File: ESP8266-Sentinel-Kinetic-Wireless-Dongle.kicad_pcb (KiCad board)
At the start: 2 copper layers, 39.7 x 60.1 mm, 61 parts, among them J1 Conn_01x04, J2 Screw_Terminal_01x04, J3 Conn_01x06_Pin, J4 RJ9, J5 Screw_Terminal_01x03, J6 Screw_Terminal_01x04, Q1 SS8050, Q2 AO3401A, Q3 AO3400A, SW2 SW_Push, SW4 SW_Push, U1 AMS1117-3.3, U2 ESP-12E, U3 MAX3232, U4 ESP32-WROOM-32, U5 L78L10_SOT89, U6 74AHCT125

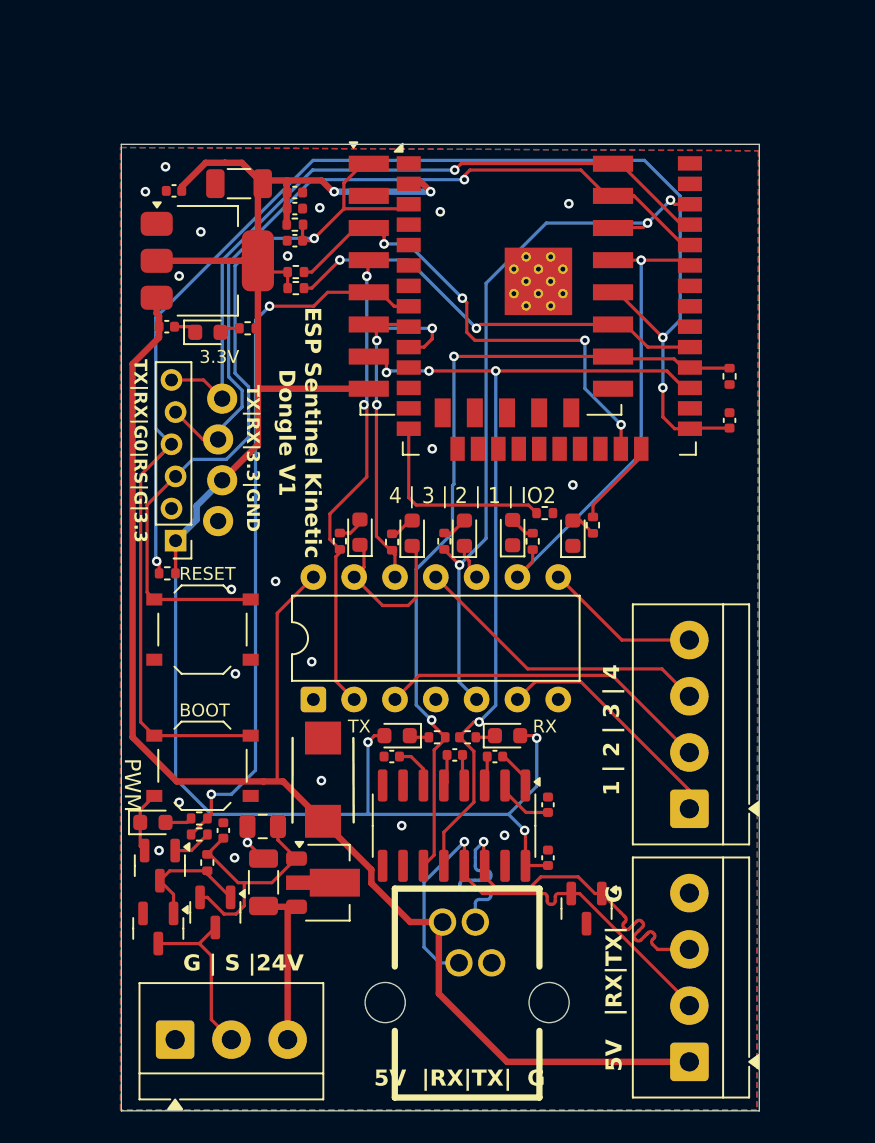
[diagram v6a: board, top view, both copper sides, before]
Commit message: Layout completed Revesed RJ9 pinout to match Display Module Added reverse polarity protection diode to 24V rail Using OpAMP for 3.3 to 5V conversion Using OpAmp for 3.3 to 10V conversion JST XH for Mode 02 Control instead of screw terminals Added 5v 3A Buck regulator PMOD connector for spare GPIO Added I2C header
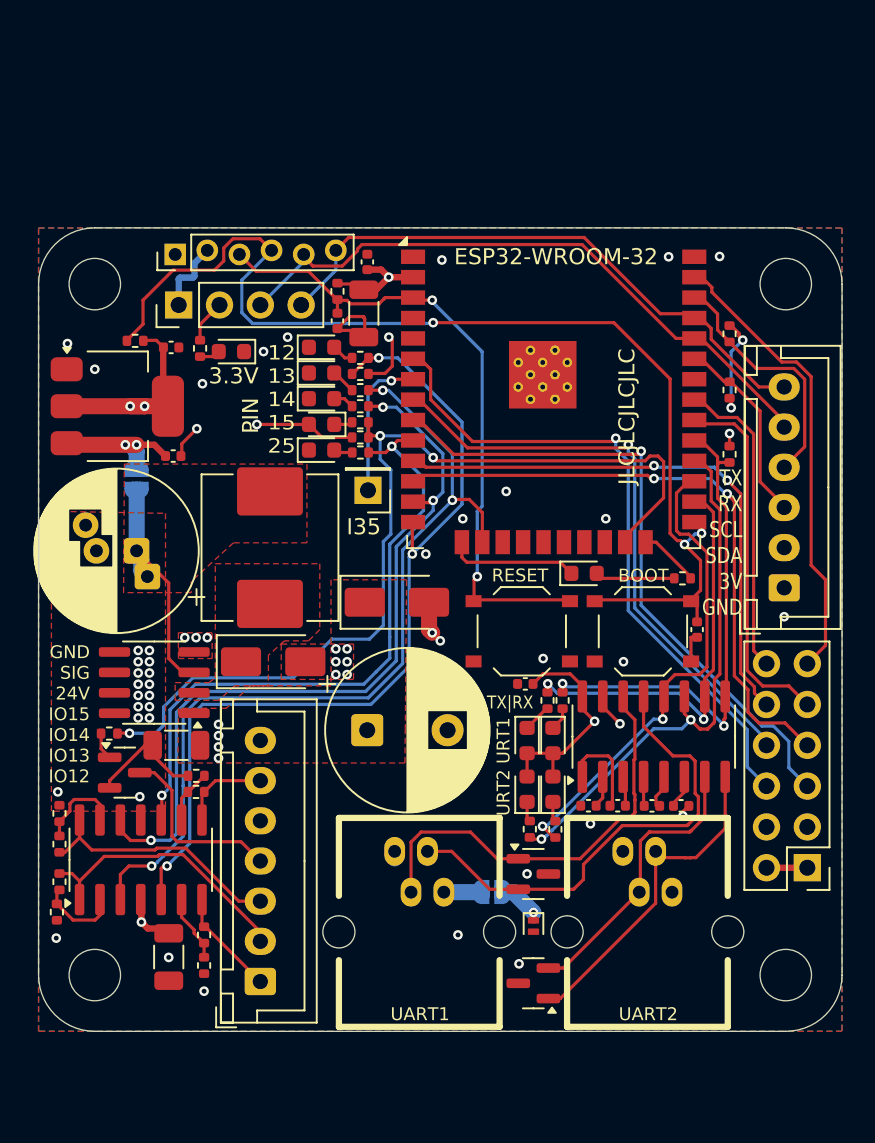
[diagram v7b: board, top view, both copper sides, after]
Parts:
- removed C14: 22uF, Capacitor_SMD:C_0805_2012Metric
- removed C15: 100n, Capacitor_SMD:C_0402_1005Metric
- removed G1: OSHW_Logo, SparkFun-Aesthetic:Creative_Commons_License
- removed Q2: AO3401A, Package_TO_SOT_SMD:SOT-23
- removed Q3: AO3400A, Package_TO_SOT_SMD:SOT-23
- removed SW4: SW_Push, Button_Switch_SMD:SW_Push_1P1T_XKB_TS-1187A
- removed U5: L78L10_SOT89, Package_TO_SOT_SMD:SOT-89-3
- removed U6: 74AHCT125, Package_DIP:DIP-14_W7.62mm
- added C16: 1u, Capacitor_SMD:C_1206_3216Metric, F.Cu at (133.6, 107.2)
- added C17: 82uF, Capacitor_THT:CP_Radial_D10.0mm_P2.50mm_P5.00mm, F.Cu at (131.1, 95.1)
- added D12: LED, LED_SMD:LED_0603_1608Metric, F.Cu at (142.6, 87.2)
- added D13: LED, LED_SMD:LED_0603_1608Metric, F.Cu at (157.0, 106.9)
- added D14: LED, LED_SMD:LED_0603_1608Metric, F.Cu at (155.4, 106.9)
- added D15: SSL34F, Diode_SMD:D_SMA, F.Cu at (139.6, 102.0)
- added D16: SSL34F, Diode_SMD:D_SMA, F.Cu at (147.3, 98.3)
- added H1: MountingHole, MountingHole:MountingHole_3.2mm_M3, F.Cu at (171.5, 78.5)
- added H2: MountingHole, MountingHole:MountingHole_3.2mm_M3, F.Cu at (171.5, 121.5)
- added H3: MountingHole, MountingHole:MountingHole_3.2mm_M3, F.Cu at (128.5, 121.5)
- added H4: MountingHole, MountingHole:MountingHole_3.2mm_M3, F.Cu at (128.5, 78.5)
- added J7: Conn_02x06_Odd_Even, Connector_PinHeader_2.54mm:PinHeader_2x06_P2.54mm_Vertical, F.Cu at (172.8, 114.8)
- added J8: Conn_01x07_Socket, Connector_JST:JST_XH_B7B-XH-A_1x07_P2.50mm_Vertical, F.Cu at (138.8, 121.9)
- added JP1: SolderJumper_2_Open, Jumper:SolderJumper-2_P1.3mm_Open_RoundedPad1.0x1.5mm, B.Cu at (153.2, 116.3)
- added JP2: SolderJumper_2_Open, Jumper:SolderJumper-2_P1.3mm_Open_RoundedPad1.0x1.5mm, B.Cu at (131.1, 90.7)
- added L1: 68uH/2A, Inductor_SMD:L_APV_APH0850, F.Cu at (139.4, 94.9)
- added R15: 10K, Resistor_SMD:R_0402_1005Metric, F.Cu at (134.8, 109.1)
- added R19: 1K, Resistor_SMD:R_0402_1005Metric, F.Cu at (157.6, 104.4)
- added R20: 1K, Resistor_SMD:R_0402_1005Metric, F.Cu at (156.7, 104.4)
- added R21: 2.2K, Resistor_SMD:R_0402_1005Metric, F.Cu at (168.0, 85.1)
- added R22: 2.2K, Resistor_SMD:R_0402_1005Metric, F.Cu at (168.0, 81.6)
- added R23: 5.1K, Resistor_SMD:R_0402_1005Metric, F.Cu at (135.3, 119.0)
- added R24: 10K, Resistor_SMD:R_0402_1005Metric, F.Cu at (126.1, 117.6)
- added R25: 5.1K, Resistor_SMD:R_0402_1005Metric, F.Cu at (126.3, 115.7)
- added R26: 10K, Resistor_SMD:R_0402_1005Metric, F.Cu at (126.3, 111.4)
- added R27: 5.1K, Resistor_SMD:R_0402_1005Metric, F.Cu at (126.3, 113.3)
- added SW1: SW_Push, Button_Switch_SMD:SW_Push_1P1T_XKB_TS-1187A, F.Cu at (155.1, 100.1)
- added U7: XL1509-5.0, Package_SO:SOIC-8_3.9x4.9mm_P1.27mm, F.Cu at (132.2, 103.3)
- C12: value 100uF -> 220uF; footprint Capacitor_SMD:C_1206_3216Metric -> Capacitor_THT:CP_Radial_D10.0mm_P5.00mm
- C13: value 10u -> 1u
- C4: value 10u -> 100uF; footprint Capacitor_SMD:C_0402_1005Metric -> Capacitor_SMD:C_1206_3216Metric
- D2: value P6SMB6.8CA-C78395 -> H5VL10B; footprint lib:SMB_L4.6-W3.6-LS5.3-BI -> Diode_SMD:D_SOD-882
- D8: value LED -> PSM712-LF-T7; footprint LED_SMD:LED_0603_1608Metric -> Package_TO_SOT_SMD:SOT-23
- J1: value Conn_01x04 -> RJ9; footprint SparkFun-Connector:1x04_Locking -> lib:RJ9-TH-623K-4P4CGRAYBOUNDLESS
- J2: value Screw_Terminal_01x04 -> RJ9; footprint TerminalBlock_4Ucon:TerminalBlock_4Ucon_1x04_P3.50mm_Horizontal -> lib:RJ9-TH-623K-4P4CGRAYBOUNDLESS
- J4: value RJ9 -> Conn_01x01_Pin; footprint lib:RJ9-TH-623K-4P4CGRAYBOUNDLESS -> Connector_PinHeader_2.54mm:PinHeader_1x01_P2.54mm_Vertical
- J5: value Screw_Terminal_01x03 -> Conn_01x04_Pin; footprint TerminalBlock_4Ucon:TerminalBlock_4Ucon_1x03_P3.50mm_Horizontal -> Connector_PinHeader_2.54mm:PinHeader_1x04_P2.54mm_Vertical
- J6: value Screw_Terminal_01x04 -> Conn_01x06_Pin; footprint TerminalBlock_4Ucon:TerminalBlock_4Ucon_1x04_P3.50mm_Horizontal -> Connector_JST:JST_XH_B6B-XH-A_1x06_P2.50mm_Vertical
- R14: value 1K -> 10K
- R16: value 1K -> 22K
- R5: value 10K -> 1K
- U2: value ESP-12E -> LM324; footprint lib:ESP-12E -> Package_SO:SOIC-14_3.9x8.7mm_P1.27mm
- moved J5 45.7 mm to (133.7, 79.8), turned to 90 degrees
- moved U2 45.4 mm to (131.4, 114.3), turned to 90 degrees
- moved C12 34.9 mm to (145.5, 106.3), turned to 0 degrees
- moved R12 28.9 mm to (129.4, 106.5), turned to 0 degrees
- moved R1 28.9 mm to (168.0, 89.1), turned to -90 degrees
- moved J4 28.8 mm to (145.5, 91.3), turned to 180 degrees
- moved SW2 28.7 mm to (162.6, 100.1)
- moved D8 28.1 mm to (155.8, 122.0), turned to 180 degrees
- moved D7 25.4 mm to (142.6, 88.8)
- moved J1 25.1 mm to (148.7, 115.1), turned to 0 degrees
- moved R11 24.9 mm to (145.0, 89.0)
- moved R5 23.2 mm to (145.0, 87.1), turned to 180 degrees
- moved C10 18.3 mm to (165.0, 111.0), turned to 0 degrees
- moved J3 17.9 mm to (133.5, 76.5), turned to 90 degrees
- moved D2 16.0 mm to (155.8, 118.5)
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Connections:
- C12 pad 1: +3.3V -> +24V
- C13 pad 1: VCC -> +24V
- D1 pad 1: /RS232_TX -> /RS_TX
- D1 pad 2: /RS232_RX -> /RS_RX
- D2 pad 1: GND -> +5V
- D2 pad 2: +5V -> GND
- D8 pad 1: GND -> /RS_RX2
- D8 pad 2: Net-(D8-A) -> /RS_TX2
- J1 pad 2: +3.3V -> /RS_TX
- J1 pad 3: /RX -> /RS_RX
- J1 pad 4: /TX -> Net-(JP1-A)
- J2 pad 1: +5V -> GND
- J2 pad 2: /RS232_RX -> /RS_TX2
- J2 pad 3: /RS232_TX -> /RS_RX2
- J2 pad 4: GND -> +5V
- J4 pad 1: +5V -> /IO35
- J5 pad 2: /10V_PWM -> +3.3V
- J5 pad 3: VCC -> /RX
- J6 pad 1: Net-(J6-Pin_1) -> GND
- J6 pad 2: Net-(J6-Pin_2) -> +3.3V
- J6 pad 3: Net-(J6-Pin_3) -> /SDA
- J6 pad 4: Net-(J6-Pin_4) -> /SCL
- Q1 pad 3: Net-(Q1-C) -> /OUT4
- R1 pad 2: /SH_1 -> /RX1
- R10 pad 1: /ALT_TX -> /TX2
- R12 pad 1: Net-(D8-A) -> Net-(Q1-B)
- R12 pad 2: /OUT1 -> /IO15
- R13 pad 2: /OUT2 -> /IO13
- R14 pad 1: /PWM -> GND
- R14 pad 2: Net-(Q1-B) -> Net-(U2B--)
- R16 pad 1: +10V -> /10V_PWM
- R16 pad 2: Net-(Q1-C) -> Net-(U2C--)
- R17 pad 2: /OUT3 -> /IO14
- R18 pad 2: /OUT4 -> /IO12
- R2 pad 2: /SH_2 -> /IO15
- R5 pad 1: GND -> /IO15
- R5 pad 2: /ALT_TX -> Net-(D12-K)
- R6 pad 2: /SL_1 -> /IO12
- R9 pad 1: /ALT_RX -> /RX2
- U2 pad 1: /RST -> /OUT2
- U2 pad 10: unconnected-(U2-MISO-Pad10) -> /PWM
- U2 pad 11: unconnected-(U2-GPIO9-Pad11) -> GND
- U2 pad 12: unconnected-(U2-GPIO10-Pad12) -> /IO14
- U2 pad 13: unconnected-(U2-MOSI-Pad13) -> Net-(U2D--)
- U2 pad 14: unconnected-(U2-SCLK-Pad14) -> /OUT3
- U2 pad 2: unconnected-(U2-ADC-Pad2) -> Net-(U2A--)
- U2 pad 3: /SH_2 -> /IO13
- U2 pad 4: /OUT4 -> +24V
- U2 pad 5: /PWM -> /IO12
- U2 pad 6: /OUT3 -> Net-(U2B--)
- U2 pad 7: /ALT_RX -> /OUT1
- U2 pad 8: +3.3V -> /10V_PWM
- U3 pad 10: GND -> /TX1
- U3 pad 11: /ALT_TX -> /TX2
- U3 pad 12: /ALT_RX -> /RX2
- U3 pad 13: /RS232_RX -> /RS_RX
- U3 pad 14: /RS232_TX -> /RS_TX
- U3 pad 7: unconnected-(U3-T2OUT-Pad7) -> /RS_TX2
- U3 pad 8: GND -> /RS_RX2
- U3 pad 9: unconnected-(U3-R2OUT-Pad9) -> /RX1
- U4 pad 10: /OUT4 -> /PWM
- U4 pad 11: unconnected-(U4-IO26-Pad11) -> /IO26
- U4 pad 12: unconnected-(U4-IO27-Pad12) -> /IO27
- U4 pad 13: unconnected-(U4-IO14-Pad13) -> /IO14
- U4 pad 14: /SL_1 -> /IO12
- U4 pad 16: unconnected-(U4-IO13-Pad16) -> /IO13
- U4 pad 23: /SH_2 -> /IO15
- U4 pad 26: unconnected-(U4-IO4-Pad26) -> /TX1
- U4 pad 27: /ALT_RX -> /RX2
- U4 pad 28: /ALT_TX -> /TX2
- U4 pad 29: /SH_1 -> /RX1
- U4 pad 30: unconnected-(U4-IO18-Pad30) -> /IO18
- U4 pad 31: unconnected-(U4-IO19-Pad31) -> /IO19
- U4 pad 33: /OUT1 -> /SDA
- U4 pad 36: /OUT2 -> /SCL
- U4 pad 37: unconnected-(U4-IO23-Pad37) -> /IO23
- U4 pad 6: unconnected-(U4-IO34-Pad6) -> /IO34
- U4 pad 7: unconnected-(U4-IO35-Pad7) -> /IO35
- U4 pad 8: /PWM -> /IO32
- U4 pad 9: /OUT3 -> /IO33
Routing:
- net /IO15: track 0.00 -> 59.1 mm, vias 0 -> 3
- net /IO12: track 0.00 -> 54.5 mm, vias 0 -> 3
- net /ALT_RX: track 54.5 -> 0.00 mm, vias 4 -> 0
- net /IO13: track 0.00 -> 54.2 mm, vias 0 -> 3
- net /ALT_TX: track 51.4 -> 0.00 mm, vias 2 -> 0
- net /IO14: track 0.00 -> 48.4 mm, vias 0 -> 3
- net +3.3V: track 118.3 -> 161.9 mm, vias 5 -> 8
- net /IO34: track 0.00 -> 41.0 mm, vias 0 -> 1
- net /IO33: track 0.00 -> 40.3 mm, vias 0 -> 1
- net /IO27: track 0.00 -> 38.8 mm, vias 0 -> 2
- net /IO32: track 0.00 -> 36.3 mm, vias 0 -> 1
- net /IO26: track 0.00 -> 34.6 mm, vias 0 -> 2
- net /TX2: track 0.00 -> 32.5 mm, vias 0 -> 2
- net /GPIO0: track 102.6 -> 71.0 mm
- net /RS232_RX: track 30.7 -> 0.00 mm, vias 1 -> 0
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- added copper zone on F.Cu, net +24V
- added copper zone on In2.Cu, net +24V
- added copper zone on In1.Cu, net GND
- added copper zone on F.Cu, net Net-(D15-K)
- added copper zone on F.Cu, net Net-(JP2-A)
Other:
- board size 39.7 x 60.1 mm -> 50 x 50 mm
- copper layers 2 -> 4
- board text added: "12 13 14 15 25"
- board text added: "5V FROM MVHR"
- board text added: "5V FROM REGULATOR"
- board text added: "5V|RX|TX|GND"
- board text added: "ESP Sentinel Kinetic Wireless Dongle V1.1 Alextrical 2025-07"
- board text added: "GND SIG 24V IO15 IO14 IO13 IO12"
- board text added: "I35"
- board text added: "IO23|IO19 IO18|IO26 IO27|IO32 IO33|I34 GND 3.3V"
- board text added: "JLCJLCJLCJLC"
- board text added: "PIN"
- board text added: "TX RX SCL SDA 3V GND"
- board text added: "TX|RX"
- board text added: "TX|RX|3V|GND"
- board text added: "TX|RX|G0|RST|GND|3V"
- board text added: "UART1"
- board text added: "UART2"
- board text added: "URT2 URT1"
- board text removed: "1 | 2 | 3 | 4"
- board text removed: "4 | 3 | 2 | 1 | IO2"
- board text removed: "5V |RX|TX| G"
- board text removed: "ESP Sentinel Kinetic Dongle V1"
- board text removed: "G | S |24V"
- board text removed: "PWM"
- board text removed: "RX"
- board text removed: "TX"
- board text removed: "TX|RX|3.3|GND"
- board text removed: "TX|RX|G0|RS|G|3.3"
